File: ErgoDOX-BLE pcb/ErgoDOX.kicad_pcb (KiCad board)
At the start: 2 copper layers, 182.8 x 158.9 mm, 118 parts, among them J1 Conn_01x04, J2 Conn_01x02_Female, J3 Conn_01x02_Female, J4 Conn_01x02, J5 Conn_01x02, J6 6PIN, P1 USB_C_Plug_USB2.0, Q1 Q_NPN_BCE, SW0:10 SW0:3, SW0:11 SW0:2, SW0:12 SW0:1, SW0:7 SW0:6, SW0:8 SW0:5, SW0:9 SW0:4, SW1:10 SW1:3, SW1:11 SW1:2, SW1:12 SW1:1, SW1:13 SW1:0, SW1:9 SW1:4, SW2:10 SW2:3, SW2:11 SW2:2, SW2:12 SW2:1, SW2:13 SW2:0, SW2:7 SW2:6, SW2:8 SW2:5, SW2:9 SW2:4, SW3:10 SW3:3, SW3:11 SW3:2, SW3:12 SW3:1, SW3:13 SW3:0, SW3:8 SW3:5, SW3:9 SW3:4, SW4:10 SW4:3, SW4:11 SW4:2, SW4:12 SW4:1, SW4:13 SW4:0, SW4:7 SW4:6, SW4:8 SW4:5, SW4:9 SW4:4, SW5:10 SW5:3, SW5:11 SW5:2, SW5:12 SW5:1, SW5:13 SW5:0, SW5:7 SW5:6, SW5:8 SW5:5, SW5:9 SW5:4, U1 MCP23018, U3 C0720B001F

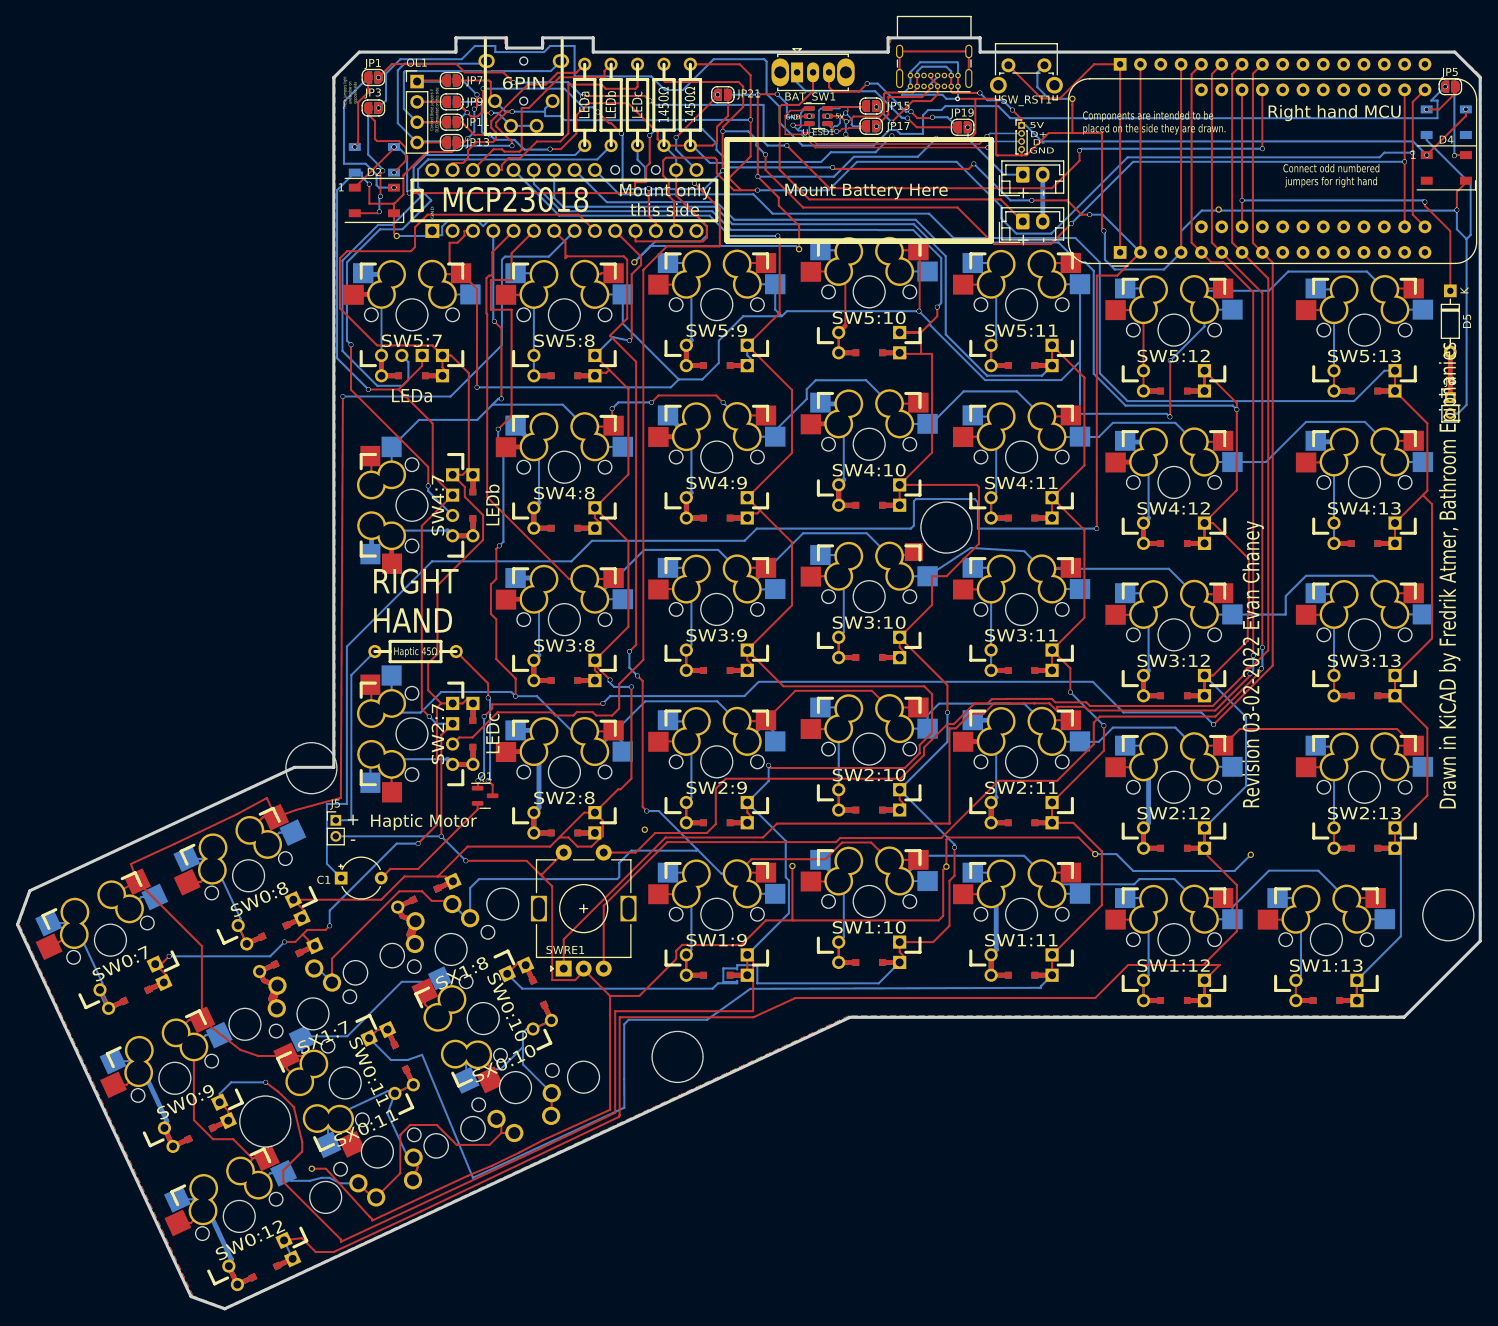
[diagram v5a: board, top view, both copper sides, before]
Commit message: Fixing overlapping footprints
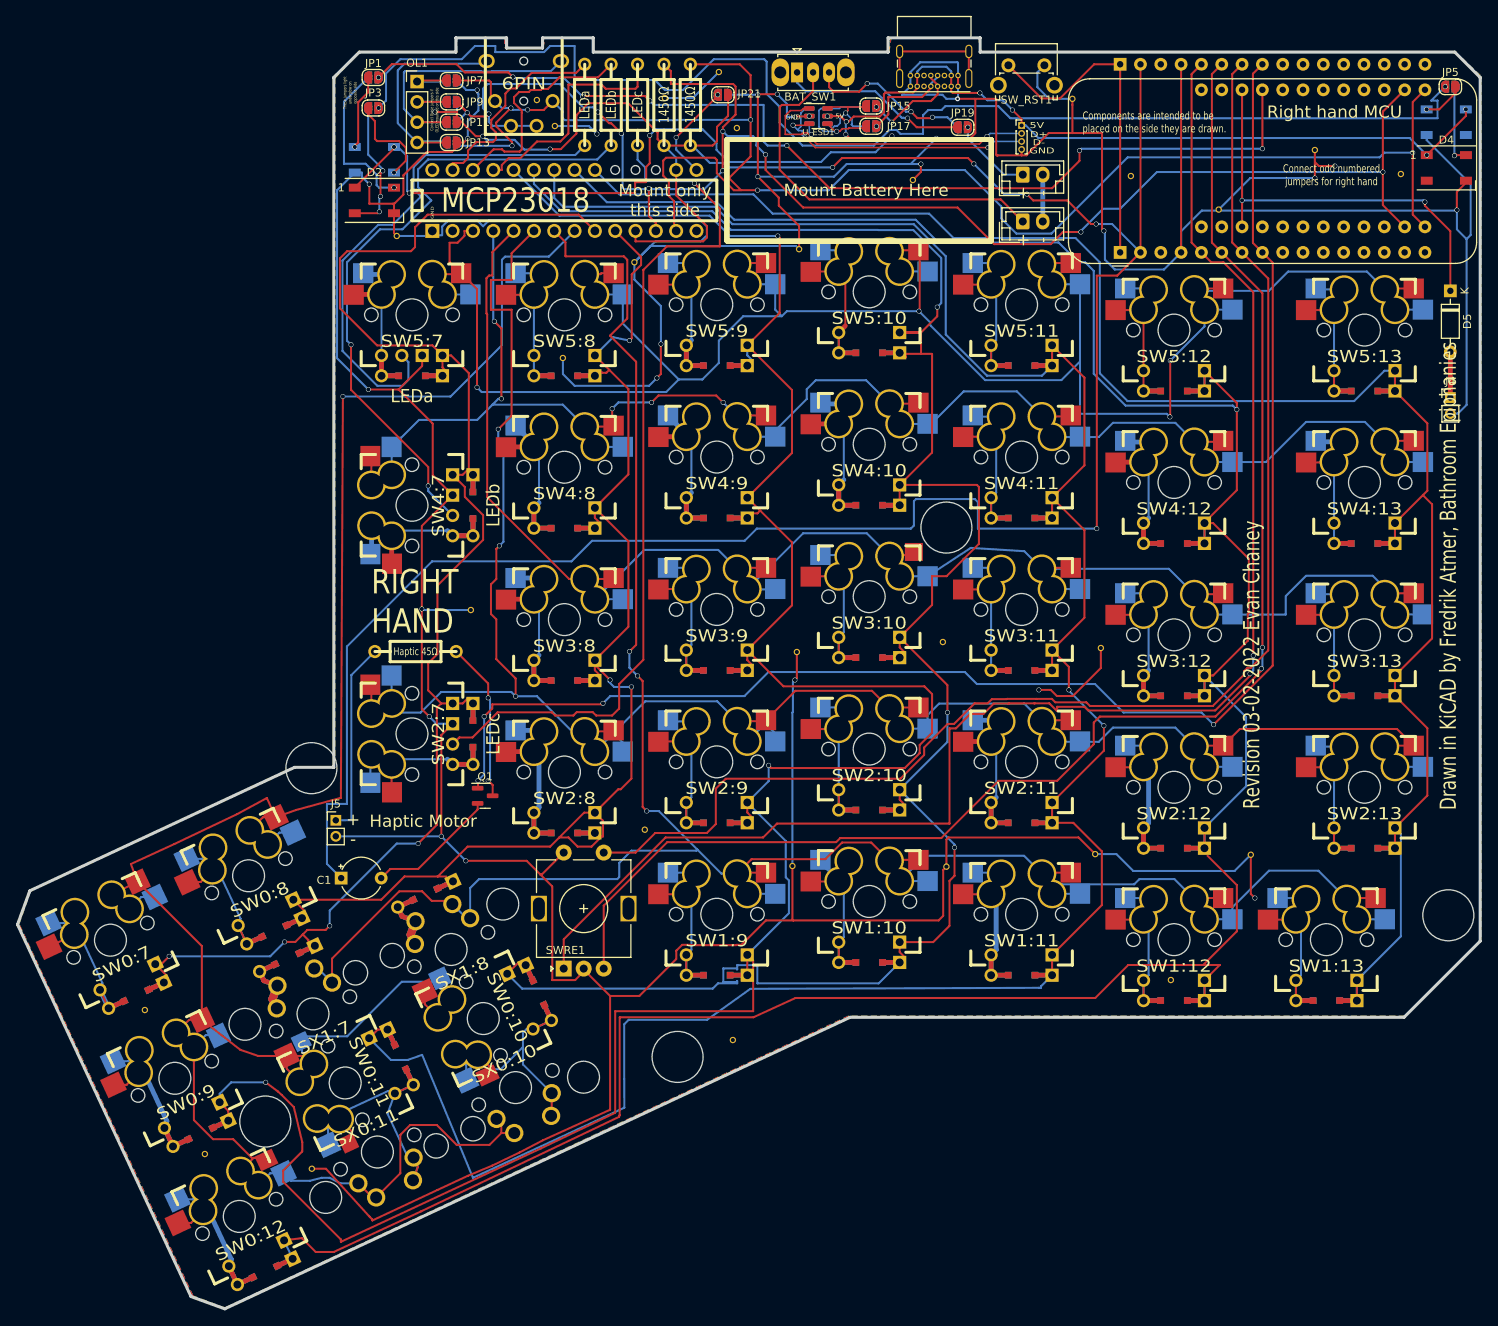
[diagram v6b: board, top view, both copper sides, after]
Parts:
- added ?: , , F.Cu at (185.2, 44.5)
- added ?: , , F.Cu at (46.5, 170.0)
- added ?: , , F.Cu at (162.2, 47.8)
- added ?: , , F.Cu at (113.0, 41.8)
- added ?: , , F.Cu at (110.8, 34.8)
- added ?: , , F.Cu at (196.0, 47.5)
- added ?: , , F.Cu at (158.5, 106.8)
- added ?: , , F.Cu at (104.0, 38.0)
- added ?: , , F.Cu at (79.8, 102.0)
- added ?: , , F.Cu at (167.2, 148.2)
- added ?: , , F.Cu at (91.2, 70.5)
- added ?: , , F.Cu at (39.0, 152.0)
- added ?: , , F.Cu at (88.0, 38.2)
- added ?: , , F.Cu at (135.0, 48.2)
- added ?: , , F.Cu at (138.8, 106.0)
- added ?: , , F.Cu at (112.5, 155.8)
- added ?: , , F.Cu at (90.2, 41.5)
- added STITCHING_VIA: ~, lib_footprints:STITCHING_VIA, F.Cu at (120.5, 107.2)
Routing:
- net GND: track 693.4 -> 812.9 mm, vias 17 -> 26
- net /LED_B: track 26.5 -> 28.2 mm
- net /SDA: track 213.1 -> 211.6 mm, vias 5 -> 6
- net /SCL: track 201.0 -> 200.0 mm, vias 11 -> 10
- net /Haptic_motor: track 191.8 -> 192.9 mm
- net /LED_A: track 25.2 -> 26.2 mm
- net +3V3: track 341.3 -> 341.0 mm, vias 7 -> 8

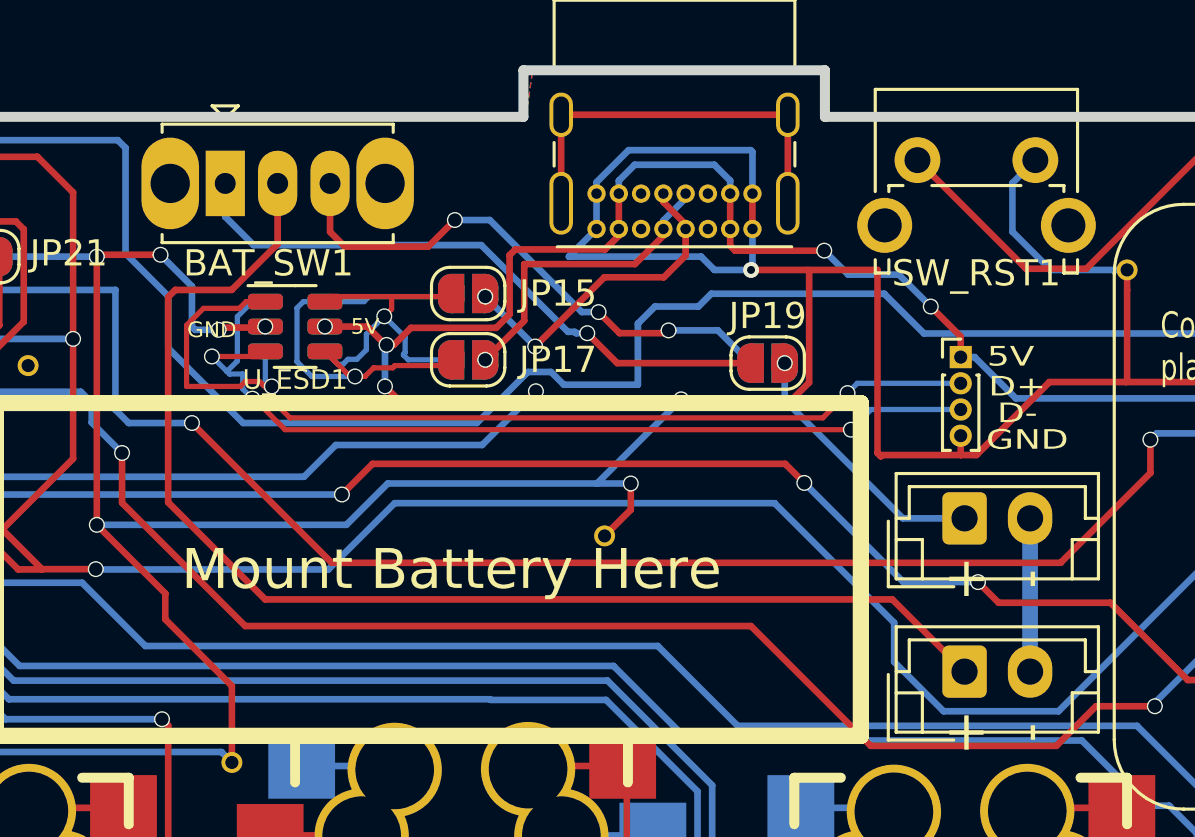
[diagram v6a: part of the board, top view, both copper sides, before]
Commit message: Adding a bunch of part numbers and verifying sizing
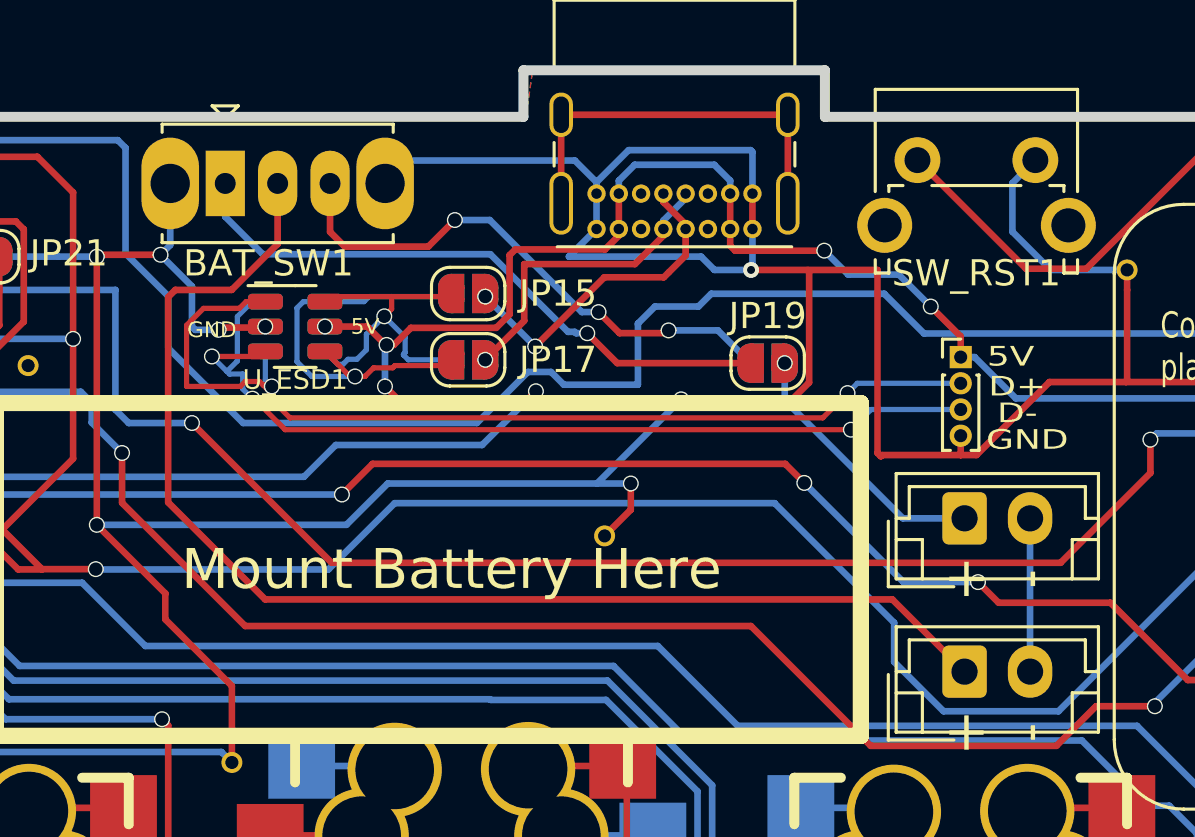
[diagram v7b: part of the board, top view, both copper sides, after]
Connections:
- BAT_SW1 pad : (no net) -> GND
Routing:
- net GND: track 812.9 -> 824.5 mm
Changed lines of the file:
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@@
     (fp_line (start 6.3 2.15) (end -2.3 2.15) (layer "F.Fab") (width 0.1))
     (fp_line (start 1.34 -1) (end 1.34 1) (layer "F.Fab") (width 0.1))
-    (pad "" thru_hole oval (at -2.1 0) (size 2.2 3.5) (drill 1.5) (layers *.Cu *.Mask))
-    (pad "" thru_hole oval (at 6.1 0) (size 2.2 3.5) (drill 1.5) (layers *.Cu *.Mask))
+    (pad "" thru_hole oval (at -2.1 0) (size 2.2 3.5) (drill 1.5) (layers *.Cu *.Mask)
+      (net 15 "GND"))
+    (pad "" thru_hole oval (at 6.1 0) (size 2.2 3.5) (drill 1.5) (layers *.Cu *.Mask)
+      (net 15 "GND"))
     (pad "1" thru_hole rect (at 0 0) (size 1.5 2.5) (drill 0.8) (layers *.Cu *.Mask)
       (net 133 "Net-(BAT_SW1-Pad1)") (pinfunction "A") (pintype "passive"))
@@
   (via (at 79.367169 43.060831) (size 0.6096) (drill 0.508) (layers "F.Cu" "B.Cu") (net 15))
   (via (at 115.621421 47.827577) (size 0.6096) (drill 0.508) (layers "F.Cu" "B.Cu") (net 15))
-  (segment (start 134.693 35.187) (end 134.693 34.752442) (width 0.254) (layer "B.Cu") (net 15))
   (segment (start 151.439 33.909) (end 150.564001 34.783999) (width 0.254) (layer "B.Cu") (net 15))
   (segment (start 66.13 47.32) (end 65.241 47.32) (width 0.254) (layer "B.Cu") (net 15))
+  (segment (start 134.693 34.752442) (end 134.693 35.187) (width 0.254) (layer "B.Cu") (net 15))
   (segment (start 114.158 37.592) (end 111.902 37.592) (width 0.254) (layer "B.Cu") (net 15))
   (segment (start 120.142 40.386) (end 120.269 40.386) (width 0.254) (layer "B.Cu") (net 15))
@@
   (segment (start 79.121 133.35) (end 76.057 130.286) (width 0.254) (layer "B.Cu") (net 15))
   (segment (start 76.057 130.286) (end 62.865 130.286) (width 0.254) (layer "B.Cu") (net 15))
+  (segment (start 118.423 37.152) (end 118.054331 37.520669) (width 0.254) (layer "B.Cu") (net 15))
   (segment (start 94.5 41.5) (end 95.5 42.5) (width 0.254) (layer "B.Cu") (net 15))
   (segment (start 203 52) (end 203 54.41) (width 0.254) (layer "B.Cu") (net 15))
   (segment (start 80.5439 37.3378) (end 80.6912 37.4851) (width 0.254) (layer "B.Cu") (net 15))
   (segment (start 102.0225 73.9775) (end 92.7275 73.9775) (width 0.254) (layer "B.Cu") (net 15))
+  (segment (start 118.423 34.798) (end 118.423 37.152) (width 0.254) (layer "B.Cu") (net 15))
   (segment (start 160.45 132.51) (end 162.56 134.62) (width 0.254) (layer "B.Cu") (net 15))
   (segment (start 73.75 102) (end 79.75 102) (width 0.254) (layer "B.Cu") (net 15))
@@
   (segment (start 80.6912 37.4851) (end 80.6912 39.5588) (width 0.254) (layer "B.Cu") (net 15))
   (segment (start 150.564001 36.641992) (end 152.022009 38.1) (width 0.254) (layer "B.Cu") (net 15))
+  (segment (start 127.4958 33.9252) (end 133.865758 33.9252) (width 0.254) (layer "B.Cu") (net 15))
   (segment (start 76.1619 54.068167) (end 76.1619 55.151833) (width 0.254) (layer "B.Cu") (net 15))
   (segment (start 202.93 52.07) (end 171.115003 52.07) (width 0.254) (layer "B.Cu") (net 15))
@@
   (segment (start 109.2581 54.068167) (end 108.491833 53.3019) (width 0.254) (layer "B.Cu") (net 15))
   (segment (start 74.93 54.61) (end 74.294999 55.245001) (width 0.254) (layer "B.Cu") (net 15))
+  (segment (start 126.623 34.798) (end 127.4958 33.9252) (width 0.254) (layer "B.Cu") (net 15))
   (segment (start 177.171 48) (end 185.25 48) (width 0.254) (layer "B.Cu") (net 15))
   (segment (start 140.57 33.528) (end 140.643 33.601) (width 0.254) (layer "B.Cu") (net 15))
   (segment (start 140.589 38.1) (end 139.192 38.1) (width 0.254) (layer "B.Cu") (net 15))
   (segment (start 80.5439 37) (end 80.5439 37.3378) (width 0.254) (layer "B.Cu") (net 15))
+  (segment (start 133.865758 33.9252) (end 134.693 34.752442) (width 0.254) (layer "B.Cu") (net 15))
   (segment (start 79.179 37) (end 77.993 35.814) (width 0.254) (layer "B.Cu") (net 15))
   (segment (start 120 111) (end 120.25 110.75) (width 0.254) (layer "B.Cu") (net 15))
@@
   (segment (start 134.338996 40.5139) (end 135.481096 41.656) (width 0.254) (layer "F.Cu") (net 133))
   (via (at 134.338996 40.5139) (size 0.6096) (drill 0.508) (layers "F.Cu" "B.Cu") (net 133))
-  (segment (start 133.602761 40.463028) (end 130.292053 37.15232) (width 0.254) (layer "B.Cu") (net 133))
+  (segment (start 133.602761 40.463028) (end 130.639733 37.5) (width 0.254) (layer "B.Cu") (net 133))
+  (segment (start 121.955 37.5) (end 120.523 36.068) (width 0.254) (layer "B.Cu") (net 133))
   (segment (start 134.338996 40.5139) (end 133.911217 40.5139) (width 0.254) (layer "B.Cu") (net 133))
+  (segment (start 133.860345 40.463028) (end 133.602761 40.463028) (width 0.254) (layer "B.Cu") (net 133))
   (segment (start 133.911217 40.5139) (end 133.860345 40.463028) (width 0.254) (layer "B.Cu") (net 133))
-  (segment (start 121.60732 37.15232) (end 120.523 36.068) (width 0.254) (layer "B.Cu") (net 133))
-  (segment (start 130.292053 37.15232) (end 121.60732 37.15232) (width 0.254) (layer "B.Cu") (net 133))
   (segment (start 120.523 36.068) (end 120.523 34.798) (width 0.254) (layer "B.Cu") (net 133))
-  (segment (start 133.860345 40.463028) (end 133.602761 40.463028) (width 0.254) (layer "B.Cu") (net 133))
-  (segment (start 151.237 47.579) (end 151.237 53.429) (width 0.6) (layer "B.Cu") (net 134))
+  (segment (start 130.639733 37.5) (end 121.955 37.5) (width 0.254) (layer "B.Cu") (net 133))
+  (segment locked (start 151.237 47.579) (end 151.237 53.429) (width 0.254) (layer "B.Cu") (net 134))
   (segment (start 118.618 38.862) (end 120.770231 38.862) (width 0.254) (layer "F.Cu") (net 135))
   (segment (start 148.737 53.429) (end 145.981 50.673) (width 0.254) (layer "F.Cu") (net 135))
